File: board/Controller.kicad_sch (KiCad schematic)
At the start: 13 parts

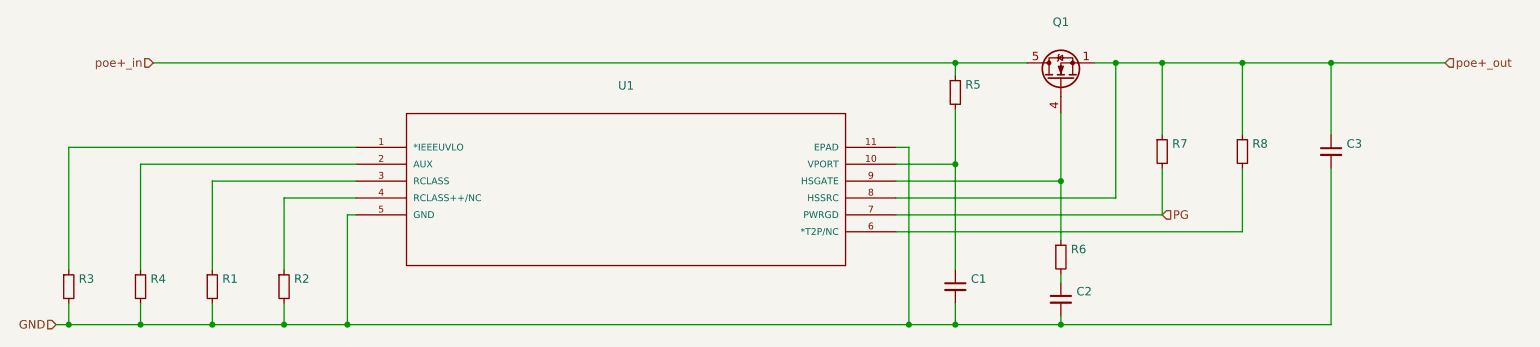
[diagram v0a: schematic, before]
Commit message: changed fp Q1 to back
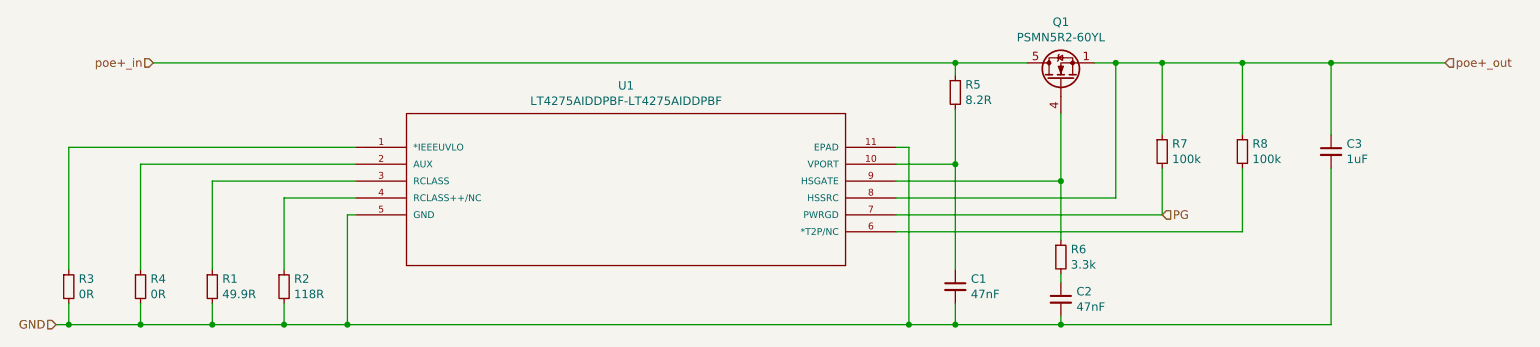
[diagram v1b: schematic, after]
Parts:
- C1, C2: value (none) -> 47nF; footprint (none) -> Capacitor_SMD:C_0603_1608Metric
- C3: value (none) -> 1uF; footprint (none) -> Capacitor_SMD:C_1206_3216Metric
- Q1: value (none) -> PSMN5R2-60YL; footprint (none) -> Package_TO_SOT_SMD:LFPAK56
- R1: value (none) -> 49.9R; footprint (none) -> Resistor_SMD:R_0603_1608Metric
- R2: value (none) -> 118R; footprint (none) -> Resistor_SMD:R_0603_1608Metric
- R3, R4: value (none) -> 0R; footprint (none) -> Resistor_SMD:R_0603_1608Metric
- R5: value (none) -> 8.2R; footprint (none) -> Resistor_SMD:R_0603_1608Metric
- R6: value (none) -> 3.3k; footprint (none) -> Resistor_SMD:R_0603_1608Metric
- R7, R8: value (none) -> 100k; footprint (none) -> Resistor_SMD:R_0603_1608Metric
- U1: value (none) -> LT4275AIDDPBF-LT4275AIDDPBF; footprint (none) -> Package_DFN_QFN:DFN-10-1EP_3x3mm_P0.5mm_EP1.65x2.38mm
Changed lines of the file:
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@@
     (in_bom yes) (on_board yes)
     (property "Reference" "U1" (id 0) (at 104.14 91.059 0))
-    (property "Value" "" (id 1) (at 104.14 93.3704 0))
-    (property "Footprint" "" (id 2) (at 63.5 100.33 0)
+    (property "Value" "LT4275AIDDPBF-LT4275AIDDPBF" (id 1) (at 104.14 93.3704 0))
+    (property "Footprint" "Package_DFN_QFN:DFN-10-1EP_3x3mm_P0.5mm_EP1.65x2.38mm" (id 2) (at 63.5 100.33 0)
       (effects (font (size 1.27 1.27)) (justify left bottom) hide)
     )
@@
       (effects (font (size 1.27 1.27)) (justify left))
     )
-    (property "Value" "" (id 1) (at 54.2036 122.428 0)
-      (effects (font (size 1.27 1.27)) (justify left))
-    )
-    (property "Footprint" "" (id 2) (at 52.705 121.285 0)
+    (property "Value" "118R" (id 1) (at 54.2036 122.428 0)
+      (effects (font (size 1.27 1.27)) (justify left))
+    )
+    (property "Footprint" "Resistor_SMD:R_0603_1608Metric" (id 2) (at 52.705 121.285 0)
       (effects (font (size 1.27 1.27)) hide)
     )
@@
       (effects (font (size 1.27 1.27)) (justify left))
     )
-    (property "Value" "" (id 1) (at 43.4086 122.428 0)
-      (effects (font (size 1.27 1.27)) (justify left))
-    )
-    (property "Footprint" "" (id 2) (at 41.91 121.285 0)
+    (property "Value" "49.9R" (id 1) (at 43.4086 122.428 0)
+      (effects (font (size 1.27 1.27)) (justify left))
+    )
+    (property "Footprint" "Resistor_SMD:R_0603_1608Metric" (id 2) (at 41.91 121.285 0)
       (effects (font (size 1.27 1.27)) hide)
     )
@@
       (effects (font (size 1.27 1.27)) (justify left))
     )
-    (property "Value" "" (id 1) (at 32.6136 122.428 0)
-      (effects (font (size 1.27 1.27)) (justify left))
-    )
-    (property "Footprint" "" (id 2) (at 31.115 121.285 0)
+    (property "Value" "0R" (id 1) (at 32.6136 122.428 0)
+      (effects (font (size 1.27 1.27)) (justify left))
+    )
+    (property "Footprint" "Resistor_SMD:R_0603_1608Metric" (id 2) (at 31.115 121.285 0)
       (effects (font (size 1.27 1.27)) hide)
     )
@@
       (effects (font (size 1.27 1.27)) (justify left))
     )
-    (property "Value" "" (id 1) (at 21.8186 122.428 0)
-      (effects (font (size 1.27 1.27)) (justify left))
-    )
-    (property "Footprint" "" (id 2) (at 20.32 121.285 0)
+    (property "Value" "0R" (id 1) (at 21.8186 122.428 0)
+      (effects (font (size 1.27 1.27)) (justify left))
+    )
+    (property "Footprint" "Resistor_SMD:R_0603_1608Metric" (id 2) (at 20.32 121.285 0)
       (effects (font (size 1.27 1.27)) hide)
     )
@@
       (effects (font (size 1.27 1.27)) (justify left))
     )
-    (property "Value" "" (id 1) (at 155.1686 93.218 0)
-      (effects (font (size 1.27 1.27)) (justify left))
-    )
-    (property "Footprint" "" (id 2) (at 153.67 92.075 0)
+    (property "Value" "8.2R" (id 1) (at 155.1686 93.218 0)
+      (effects (font (size 1.27 1.27)) (justify left))
+    )
+    (property "Footprint" "Resistor_SMD:R_0603_1608Metric" (id 2) (at 153.67 92.075 0)
       (effects (font (size 1.27 1.27)) hide)
     )
@@
       (effects (font (size 1.27 1.27)) (justify left))
     )
-    (property "Value" "" (id 1) (at 156.0068 122.428 0)
-      (effects (font (size 1.27 1.27)) (justify left))
-    )
-    (property "Footprint" "" (id 2) (at 153.67 121.285 0)
+    (property "Value" "47nF" (id 1) (at 156.0068 122.428 0)
+      (effects (font (size 1.27 1.27)) (justify left))
+    )
+    (property "Footprint" "Capacitor_SMD:C_0603_1608Metric" (id 2) (at 153.67 121.285 0)
       (effects (font (size 1.27 1.27)) hide)
     )
@@
     (in_bom yes) (on_board yes)
     (property "Reference" "Q1" (id 0) (at 169.545 81.4832 90))
-    (property "Value" "" (id 1) (at 169.545 83.7946 90))
-    (property "Footprint" "" (id 2) (at 169.545 86.36 0)
+    (property "Value" "PSMN5R2-60YL" (id 1) (at 169.545 83.7946 90))
+    (property "Footprint" "Package_TO_SOT_SMD:LFPAK56" (id 2) (at 169.545 86.36 0)
       (effects (font (size 1.27 1.27)) hide)
     )
@@
       (effects (font (size 1.27 1.27)) (justify left))
     )
-    (property "Value" "" (id 1) (at 171.8818 124.333 0)
-      (effects (font (size 1.27 1.27)) (justify left))
-    )
-    (property "Footprint" "" (id 2) (at 169.545 123.19 0)
+    (property "Value" "47nF" (id 1) (at 171.8818 124.333 0)
+      (effects (font (size 1.27 1.27)) (justify left))
+    )
+    (property "Footprint" "Capacitor_SMD:C_0603_1608Metric" (id 2) (at 169.545 123.19 0)
       (effects (font (size 1.27 1.27)) hide)
     )
@@
       (effects (font (size 1.27 1.27)) (justify left))
     )
-    (property "Value" "" (id 1) (at 171.0436 117.983 0)
-      (effects (font (size 1.27 1.27)) (justify left))
-    )
-    (property "Footprint" "" (id 2) (at 169.545 116.84 0)
+    (property "Value" "3.3k" (id 1) (at 171.0436 117.983 0)
+      (effects (font (size 1.27 1.27)) (justify left))
+    )
+    (property "Footprint" "Resistor_SMD:R_0603_1608Metric" (id 2) (at 169.545 116.84 0)
       (effects (font (size 1.27 1.27)) hide)
     )
@@
       (effects (font (size 1.27 1.27)) (justify left))
     )
-    (property "Value" "" (id 1) (at 186.2836 102.108 0)
-      (effects (font (size 1.27 1.27)) (justify left))
-    )
-    (property "Footprint" "" (id 2) (at 184.785 100.965 0)
+    (property "Value" "100k" (id 1) (at 186.2836 102.108 0)
+      (effects (font (size 1.27 1.27)) (justify left))
+    )
+    (property "Footprint" "Resistor_SMD:R_0603_1608Metric" (id 2) (at 184.785 100.965 0)
       (effects (font (size 1.27 1.27)) hide)
     )
@@
       (effects (font (size 1.27 1.27)) (justify left))
     )
-    (property "Value" "" (id 1) (at 198.3486 102.108 0)
-      (effects (font (size 1.27 1.27)) (justify left))
-    )
-    (property "Footprint" "" (id 2) (at 196.85 100.965 0)
+    (property "Value" "100k" (id 1) (at 198.3486 102.108 0)
+      (effects (font (size 1.27 1.27)) (justify left))
+    )
+    (property "Footprint" "Resistor_SMD:R_0603_1608Metric" (id 2) (at 196.85 100.965 0)
       (effects (font (size 1.27 1.27)) hide)
     )
@@
       (effects (font (size 1.27 1.27)) (justify left))
     )
-    (property "Value" "" (id 1) (at 212.5218 102.108 0)
-      (effects (font (size 1.27 1.27)) (justify left))
-    )
-    (property "Footprint" "" (id 2) (at 210.185 100.965 0)
-      (effects (font (size 1.27 1.27)) hide)
-    )
+    (property "Value" "1uF" (id 1) (at 212.5218 102.108 0)
+      (effects (font (size 1.27 1.27)) (justify left))
+    )
+    (property "Footprint" "Capacitor_SMD:C_1206_3216Metric" (id 2) (at 210.185 100.965 0)
+      (effects (font (size 1.27 1.27)) hide)
+    )
